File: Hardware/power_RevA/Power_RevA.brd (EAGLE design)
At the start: 100 x 80 mm, 11 parts, among them Q1 TIP120

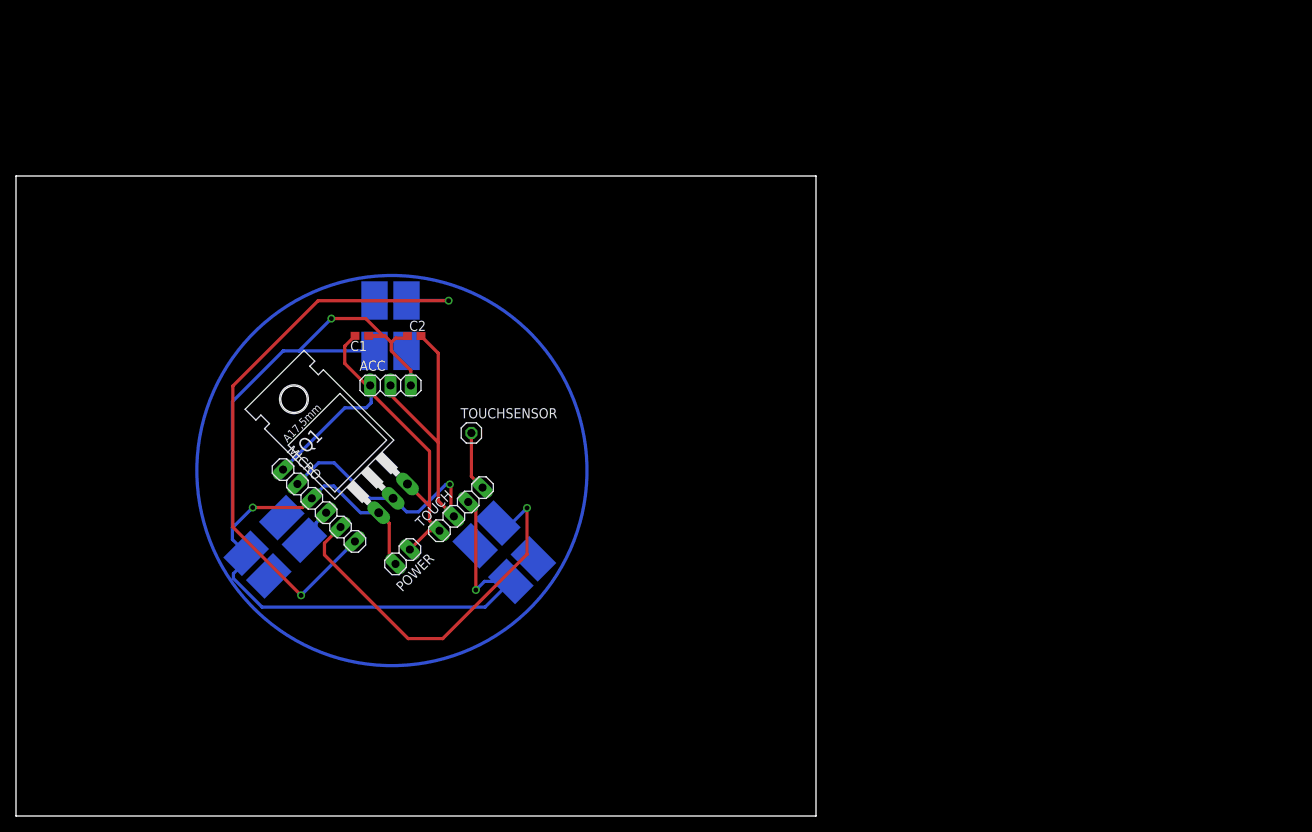
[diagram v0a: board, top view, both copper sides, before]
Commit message: Added labels, resized boundary
Everything is labeled now, but the boards needs to be placed in the 5cm
by 5cm boundary. The vias leave their holes behind though....
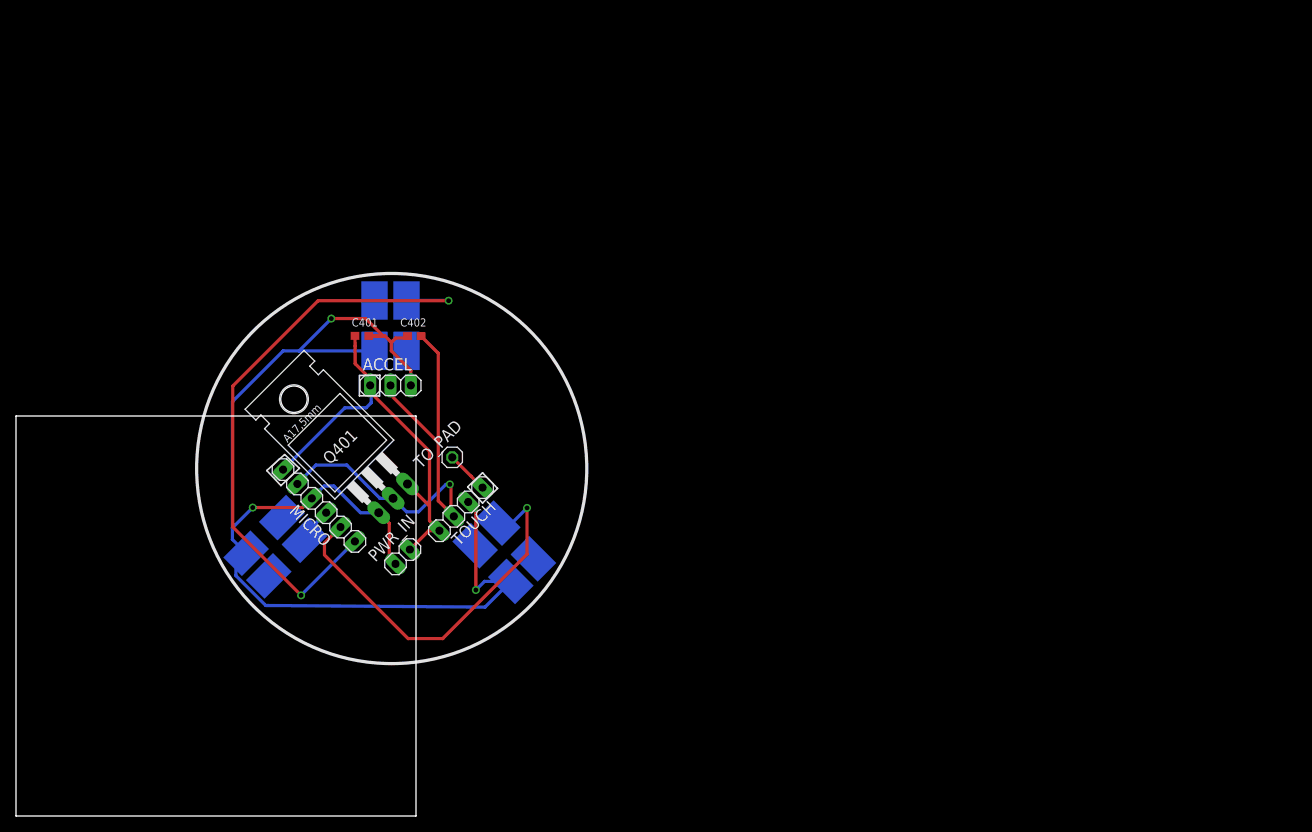
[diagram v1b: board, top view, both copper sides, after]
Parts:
- removed TOUCHSENSOR: (no value), pinhead:1X01
- added TO_PAD: (no value), pinhead:1X01
- renumbered ACC to ACCEL, C1 to C401, C2 to C402, POWER to PWR_IN, Q1 to Q401
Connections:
- net N$1: now also TO_PAD.1; no longer TOUCHSENSOR.1
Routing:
- net N$1: track 7.41 -> 5.35 mm
- net N$2: track 55.8 -> 54.4 mm
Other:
- board size 100 x 80 mm -> 50 x 50 mm

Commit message: Power and Touch Board LED Orientation Fixed
The touch board is sill routed incorrectly (schematic is wrong too) but
orientation is silk-screened on board. Power board is routed absolutely
correctly.
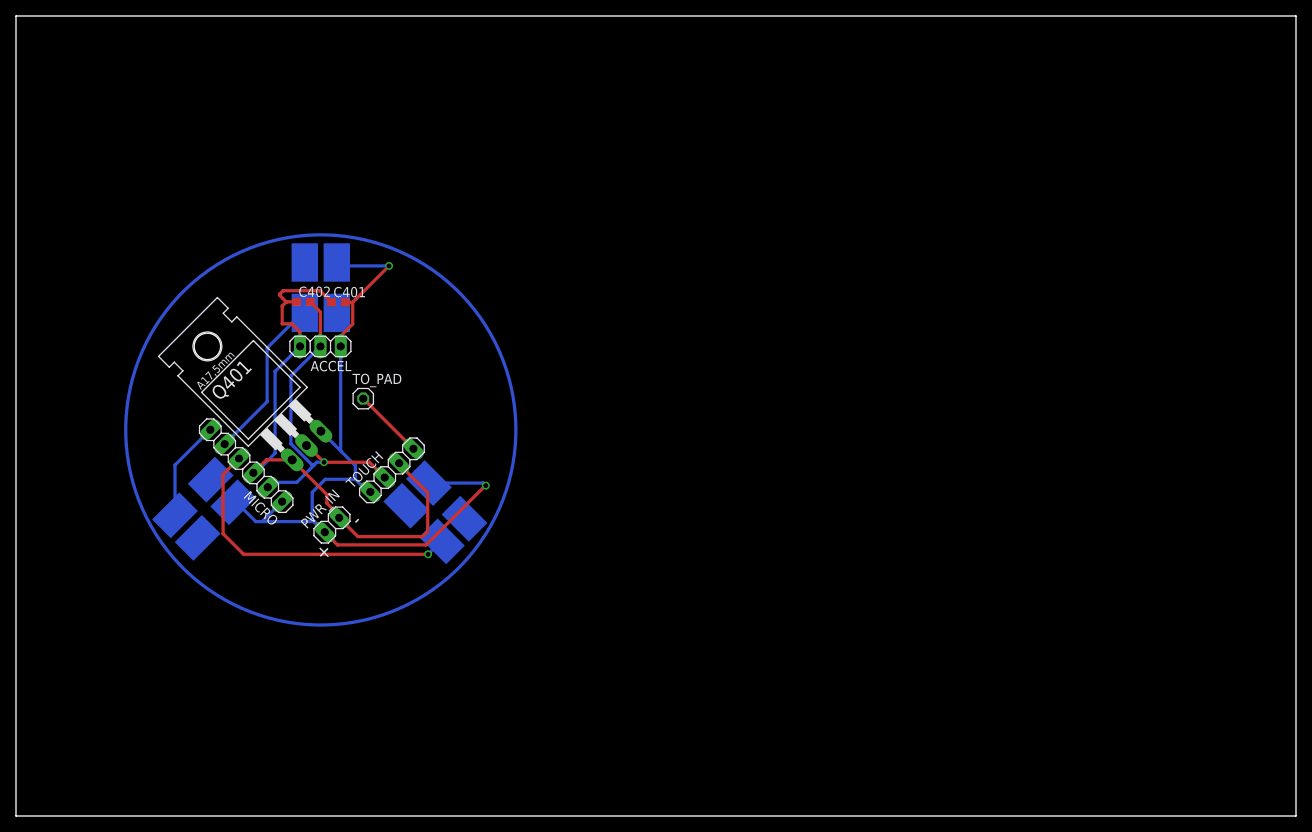
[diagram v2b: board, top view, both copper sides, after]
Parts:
- moved LED2 40.2 mm to (38.1, 66.0), turned to 0 degrees
- moved LED1 32.7 mm to (23.5, 38.4), turned to 45 degrees
- moved LED3 20.5 mm to (52.4, 38.0), turned to 315 degrees
- moved C402 14.5 mm to (35.9, 64.3)
- moved TO_PAD 13.3 mm to (43.4, 52.2)
- moved Q401 12.7 mm to (31.8, 50.8)
- moved MICRO 10.4 mm to (28.8, 43.8), turned to 135 degrees
- moved ACCEL 10.0 mm to (38.0, 58.7), turned to 180 degrees
- moved TOUCH 9.91 mm to (47.0, 43.2)
- moved PWR_IN 9.69 mm to (39.5, 36.4), turned to 45 degrees
- moved C401 5.11 mm to (40.3, 64.2), turned to 0 degrees
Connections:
- removed net N$7: LED1.A, MICRO.6
- new net N$3: LED1.C@4, MICRO.6
- net N$2: now also LED1.A, LED2.A, LED3.A
- net N$5: now also LED2.C@4, MICRO.5; no longer LED3.A, MICRO.4
- net N$6: now also LED3.C@4, MICRO.4; no longer LED2.A, MICRO.5
- net N$8: no longer LED1.C@4, LED2.C@4, LED3.C@4
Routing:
- net N$8: track 153.6 -> 73.2 mm, vias 3 -> 0
- net N$7: track 75.9 -> 0.00 mm, vias 2 -> 0
- net N$2: track 54.4 -> 102.9 mm, vias 0 -> 2
- net N$4: track 61.4 -> 43.6 mm
- net N$5: track 4.57 -> 20.7 mm
- net N$3: track 0.00 -> 12.5 mm
- net N$6: track 48.6 -> 39.3 mm
- net N$1: track 5.35 -> 8.87 mm
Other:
- board size 50 x 50 mm -> 160 x 100 mm
- board text added: "+"
- board text added: "-"
